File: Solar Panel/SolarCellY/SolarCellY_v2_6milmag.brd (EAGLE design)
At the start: 100 x 82 mm, 23 parts

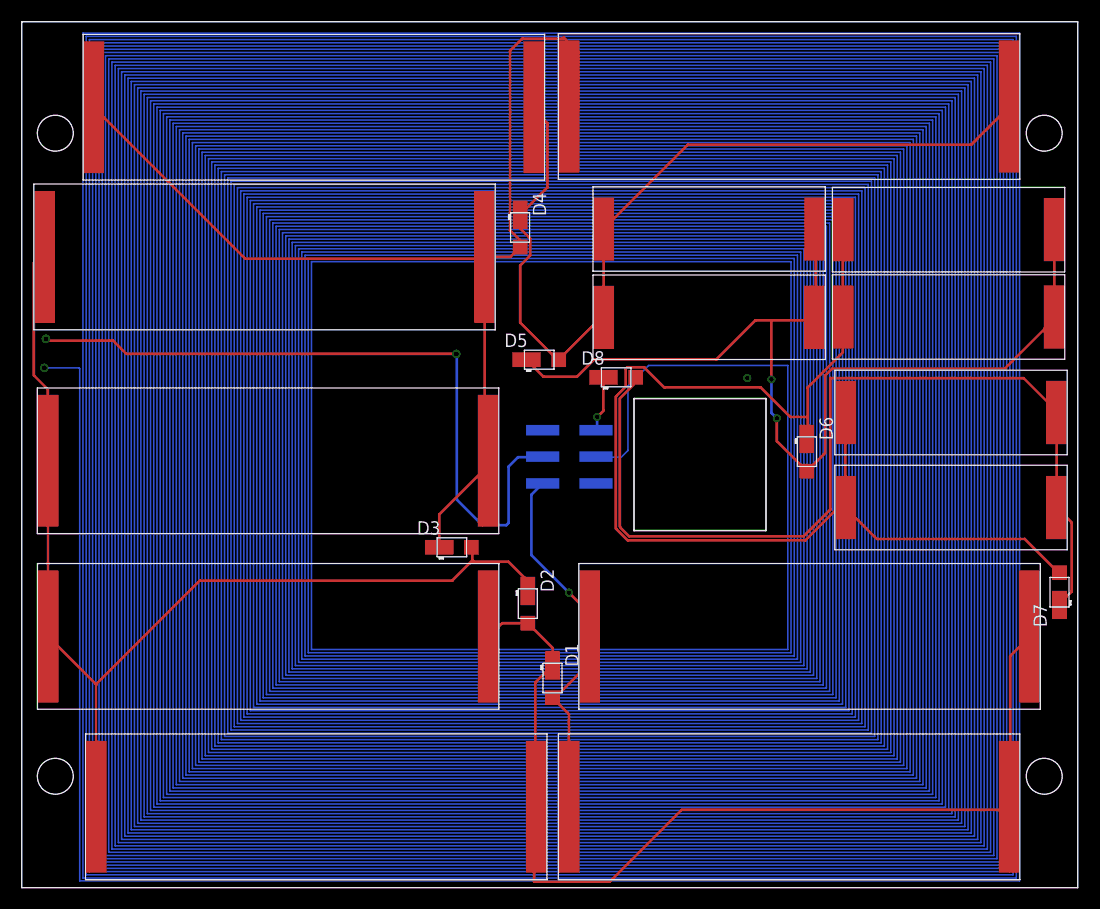
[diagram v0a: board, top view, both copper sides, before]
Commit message: Changed connector config and DRC stuff for Y panel
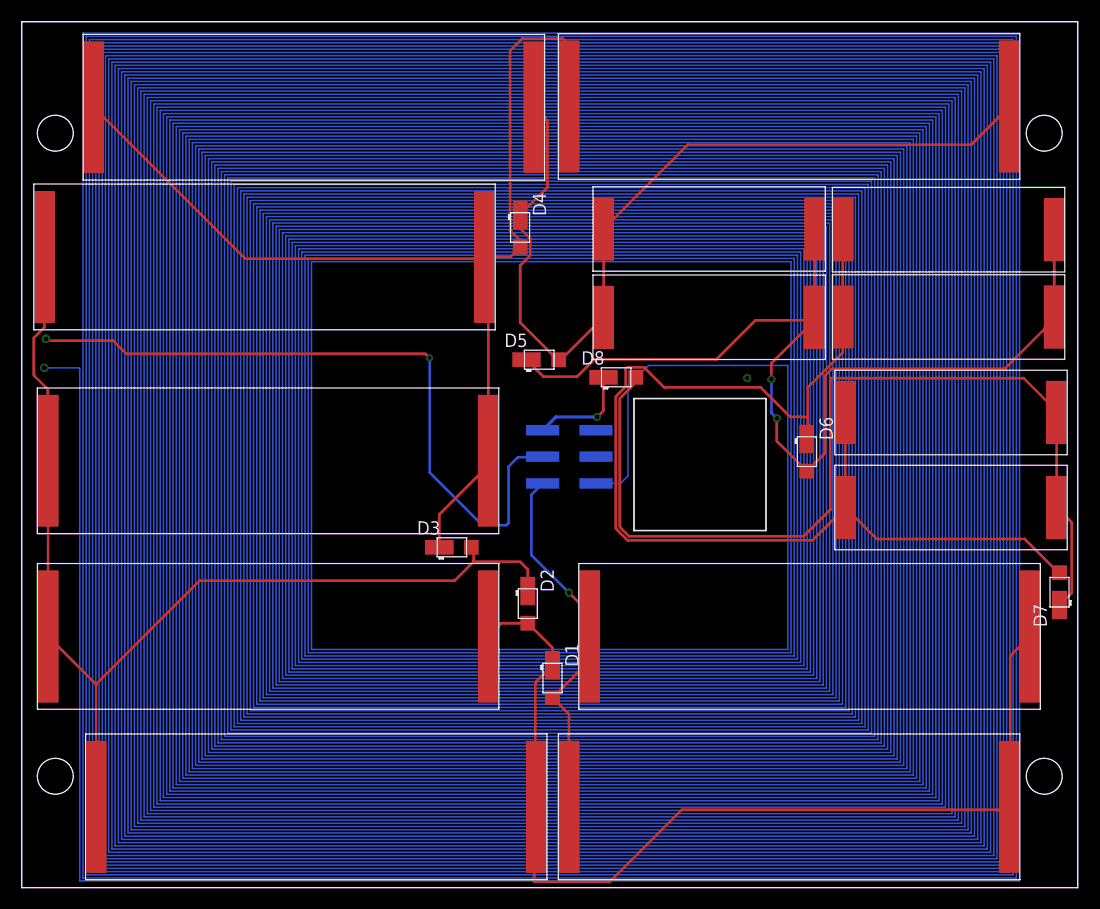
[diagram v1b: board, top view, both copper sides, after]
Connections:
- net N$1: now also U$1.P$2; no longer U$1.P$4
- net N$14: now also U$1.P$5; no longer U$1.P$6
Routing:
- net N$14: track 5.40 -> 9.68 mm
- net N$6: track 97.2 -> 98.4 mm
- net GND: track 36.1 -> 35.4 mm
